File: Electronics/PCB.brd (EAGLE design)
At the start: 39.4 x 52.1 mm, 9 parts, among them IC1 7805T

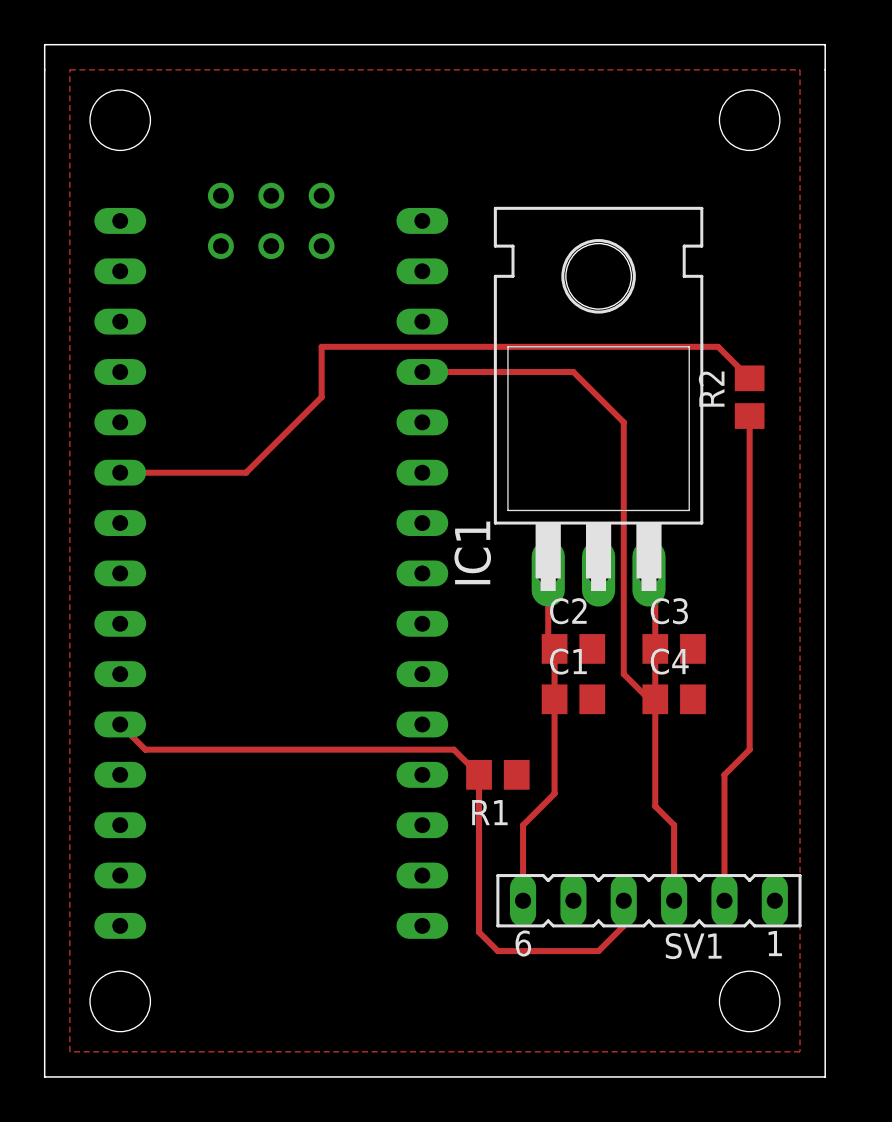
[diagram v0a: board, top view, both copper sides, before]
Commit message: changed traces to 20 mills
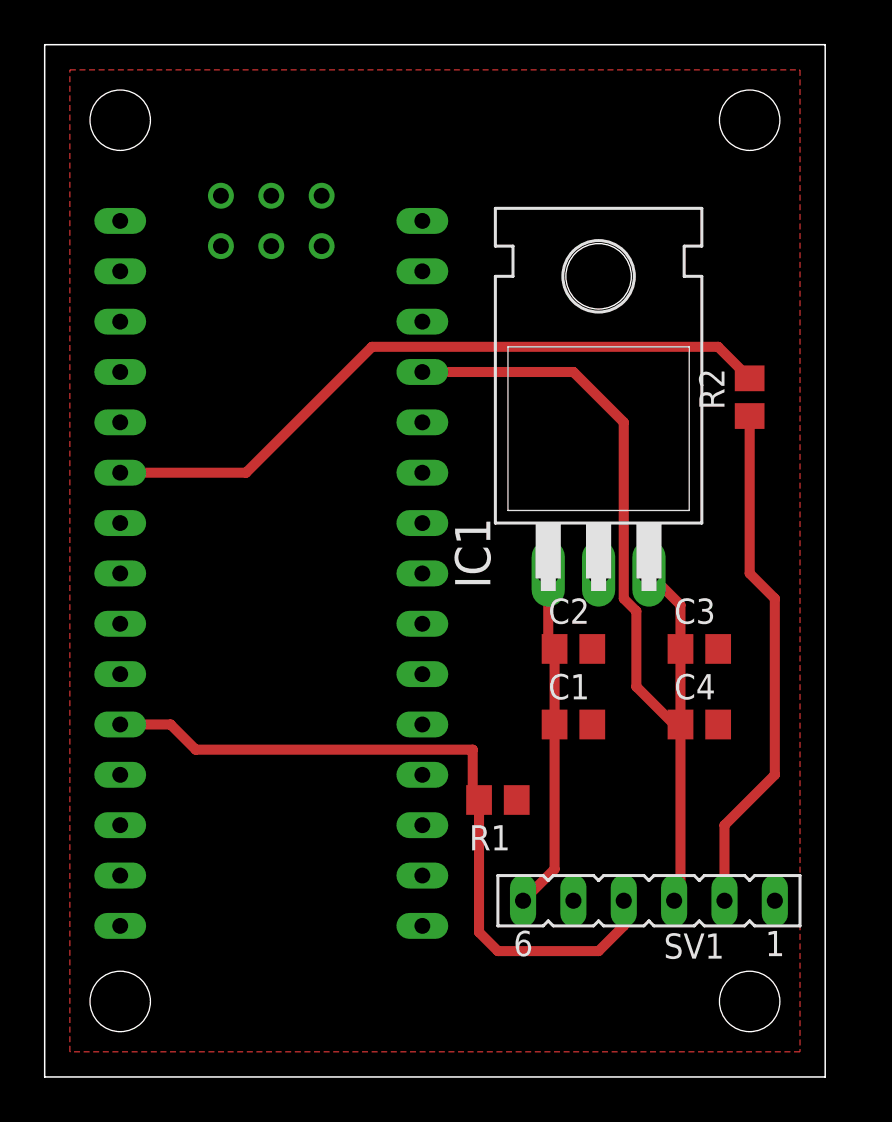
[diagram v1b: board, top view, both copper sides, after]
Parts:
- moved C4 1.80 mm to (34.3, 64.8)
- moved C1 1.27 mm to (27.9, 64.8)
- moved C3 1.27 mm to (34.3, 68.6)
- moved R1 1.27 mm to (24.1, 61.0)
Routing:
- net 5V: track 43.1 -> 45.1 mm
- net PWM: track 36.5 -> 35.0 mm
- net LIGHT: track 25.0 -> 26.0 mm
- net BUTTON: track 36.6 -> 37.1 mm
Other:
- outline, holes or cut-outs redrawn

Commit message: removed regulator, changed some pins for better routing
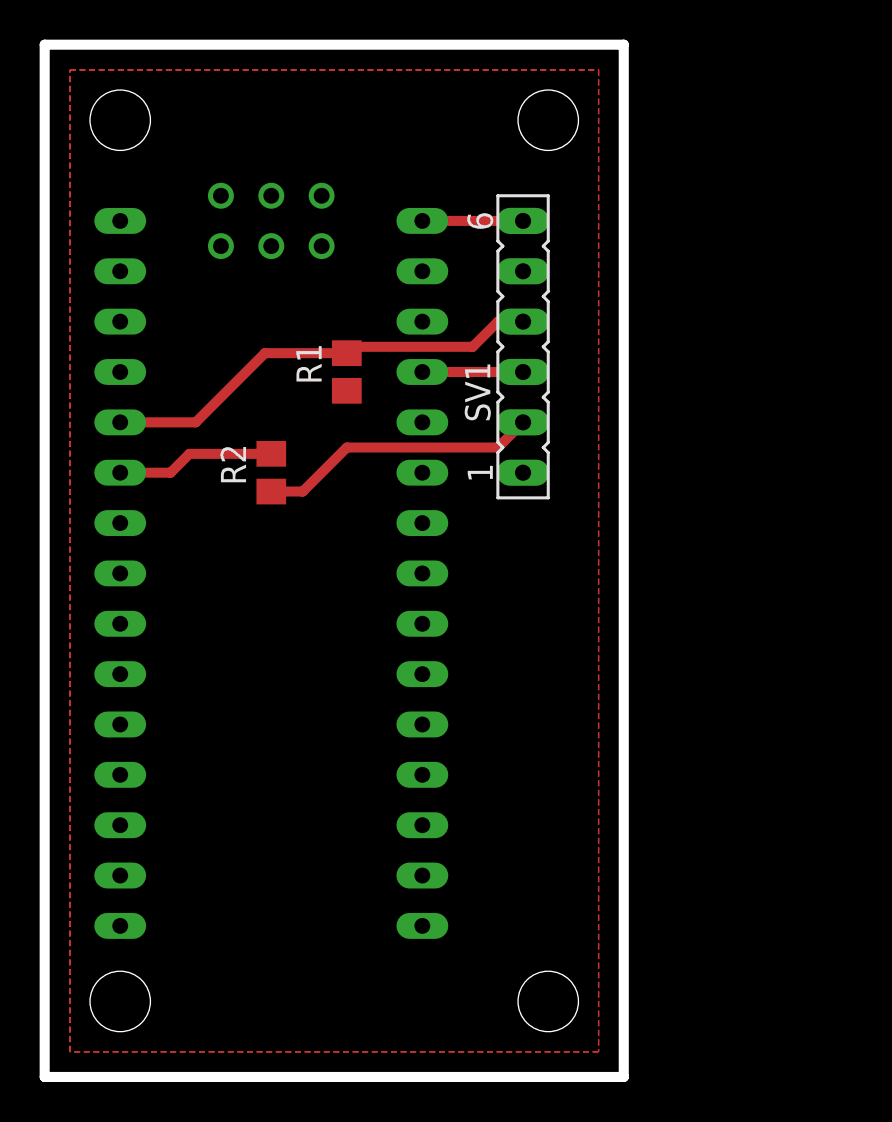
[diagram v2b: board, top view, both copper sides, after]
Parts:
- removed C1, C3: 10 uF, eagle-ltspice:C0805
- removed C2, C4: 0.1 uF, eagle-ltspice:C0805
- removed IC1: 7805T, adafruit:TO220H
- moved SV1 28.7 mm to (25.4, 83.8), turned to 90 degrees
- moved R2 24.4 mm to (12.7, 77.5)
- moved R1 22.9 mm to (16.5, 82.5), turned to 90 degrees
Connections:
- net 5V: no longer C3.1, C4.1, IC1.3
- net 9V: now also U$1.RAW; no longer C1.1, C2.1, IC1.1
- net BUTTON: now also U$1.D2; no longer U$1.D8
- net GND: no longer C1.2, C2.2, C3.2, C4.2, IC1.2
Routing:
- net 5V: track 45.1 -> 5.08 mm
- net PWM: track 35.0 -> 8.01 mm
- net BUTTON: track 37.1 -> 22.4 mm
- net 9V: track 17.5 -> 5.08 mm
- net LIGHT: track 26.0 -> 14.5 mm
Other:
- board size 39.4 x 52.1 mm -> 29.2 x 52.1 mm

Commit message: Final PCB Design
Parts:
- R2: value (none) -> 220
- moved R2 6.35 mm to (19.1, 77.5)
- moved SV1 6.35 mm to (31.8, 83.8)
- moved U$1 6.35 mm to (16.5, 81.3)
- moved R1 6.35 mm to (22.9, 82.5)
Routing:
- removed copper zone on layer 1, net GND
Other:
- board size 29.2 x 52.1 mm -> 40.6 x 52.1 mm
